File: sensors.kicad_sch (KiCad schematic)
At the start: 246 parts, among them K1 DRV5055A3xDBZxQ1, K10 DRV5055A3xDBZxQ1, K11 DRV5055A3xDBZxQ1, K12 DRV5055A3xDBZxQ1, K13 DRV5055A3xDBZxQ1, K14 DRV5055A3xDBZxQ1, K15 DRV5055A3xDBZxQ1, K16 DRV5055A3xDBZxQ1, K17 DRV5055A3xDBZxQ1, K18 DRV5055A3xDBZxQ1, K19 DRV5055A3xDBZxQ1, K2 DRV5055A3xDBZxQ1, K20 DRV5055A3xDBZxQ1, K21 DRV5055A3xDBZxQ1, K22 DRV5055A3xDBZxQ1, K23 DRV5055A3xDBZxQ1, K24 DRV5055A3xDBZxQ1, K25 DRV5055A3xDBZxQ1, K26 DRV5055A3xDBZxQ1, K27 DRV5055A3xDBZxQ1, K28 DRV5055A3xDBZxQ1, K29 DRV5055A3xDBZxQ1, K3 DRV5055A3xDBZxQ1, K30 DRV5055A3xDBZxQ1, K31 DRV5055A3xDBZxQ1, K32 DRV5055A3xDBZxQ1, K33 DRV5055A3xDBZxQ1, K34 DRV5055A3xDBZxQ1, K35 DRV5055A3xDBZxQ1, K36 DRV5055A3xDBZxQ1, K37 DRV5055A3xDBZxQ1, K38 DRV5055A3xDBZxQ1, K39 DRV5055A3xDBZxQ1, K4 DRV5055A3xDBZxQ1, K40 DRV5055A3xDBZxQ1, K41 DRV5055A3xDBZxQ1, K42 DRV5055A3xDBZxQ1, K43 DRV5055A3xDBZxQ1, K44 DRV5055A3xDBZxQ1, K45 DRV5055A3xDBZxQ1, K46 DRV5055A3xDBZxQ1, K47 DRV5055A3xDBZxQ1, K48 DRV5055A3xDBZxQ1, K49 DRV5055A3xDBZxQ1, K5 DRV5055A3xDBZxQ1, K50 DRV5055A3xDBZxQ1, K51 DRV5055A3xDBZxQ1, K52 DRV5055A3xDBZxQ1, K53 DRV5055A3xDBZxQ1, K54 DRV5055A3xDBZxQ1, K55 DRV5055A3xDBZxQ1, K56 DRV5055A3xDBZxQ1, K57 DRV5055A3xDBZxQ1, K58 DRV5055A3xDBZxQ1, K59 DRV5055A3xDBZxQ1, K6 DRV5055A3xDBZxQ1, K60 DRV5055A3xDBZxQ1, K61 DRV5055A3xDBZxQ1, K62 DRV5055A3xDBZxQ1, K63 DRV5055A3xDBZxQ1, K64 DRV5055A3xDBZxQ1, K65 DRV5055A3xDBZxQ1, K66 DRV5055A3xDBZxQ1, K67 DRV5055A3xDBZxQ1, K68 DRV5055A3xDBZxQ1, K69 DRV5055A3xDBZxQ1, K7 DRV5055A3xDBZxQ1, K70 DRV5055A3xDBZxQ1, K71 DRV5055A3xDBZxQ1, K72 DRV5055A3xDBZxQ1, K73 DRV5055A3xDBZxQ1, K74 DRV5055A3xDBZxQ1, K75 DRV5055A3xDBZxQ1, K76 DRV5055A3xDBZxQ1, K77 DRV5055A3xDBZxQ1, K78 DRV5055A3xDBZxQ1, K79 DRV5055A3xDBZxQ1, K8 DRV5055A3xDBZxQ1, K80 DRV5055A3xDBZxQ1, K81 DRV5055A3xDBZxQ1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

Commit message: add capacitor to mux vcc
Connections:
- net K1_OUT: no longer C10.2, C12.2, C14.2, C16.2, C18.2, C20.2, C22.2, C24.2, C26.2, C28.2, C30.2, C32.2, C4.2, C6.2, C8.2, K10.2 (OUT), K11.2 (OUT), K12.2 (OUT), K13.2 (OUT), K14.2 (OUT), K15.2 (OUT), K16.2 (OUT), K2.2 (OUT), K3.2 (OUT), K4.2 (OUT), K5.2 (OUT), K6.2 (OUT), K7.2 (OUT), K8.2 (OUT), K9.2 (OUT)
- new net K10_OUT: C20.2, K10.2 (OUT)
- new net K11_OUT: C22.2, K11.2 (OUT)
- new net K12_OUT: C24.2, K12.2 (OUT)
- new net K13_OUT: C26.2, K13.2 (OUT)
- new net K14_OUT: C28.2, K14.2 (OUT)
- new net K15_OUT: C30.2, K15.2 (OUT)
- new net K16_OUT: C32.2, K16.2 (OUT)
- new net K2_OUT: C4.2, K2.2 (OUT)
- new net K3_OUT: C6.2, K3.2 (OUT)
- new net K4_OUT: C8.2, K4.2 (OUT)
- new net K5_OUT: C10.2, K5.2 (OUT)
- new net K6_OUT: C12.2, K6.2 (OUT)
- new net K7_OUT: C14.2, K7.2 (OUT)
- new net K8_OUT: C16.2, K8.2 (OUT)
- new net K9_OUT: C18.2, K9.2 (OUT)
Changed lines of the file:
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@@
 		)
 	)
-	(global_label "K1_OUT"
+	(global_label "K16_OUT"
 		(shape input)
 		(at 417.83 68.58 90)
@@
 		)
 		(property "Intersheetrefs" "${INTERSHEET_REFS}"
-			(at 417.83 58.5191 90)
-			(effects
-				(font
-					(size 1.27 1.27)
-				)
-				(justify left)
-				(hide yes)
-			)
-		)
-	)
-	(global_label "K1_OUT"
+			(at 417.83 57.3096 90)
+			(effects
+				(font
+					(size 1.27 1.27)
+				)
+				(justify left)
+				(hide yes)
+			)
+		)
+	)
+	(global_label "K3_OUT"
 		(shape input)
 		(at 162.56 31.75 90)
@@
 		)
 	)
-	(global_label "K1_OUT"
+	(global_label "K15_OUT"
 		(shape input)
 		(at 367.03 68.58 90)
@@
 		)
 		(property "Intersheetrefs" "${INTERSHEET_REFS}"
-			(at 367.03 58.5191 90)
+			(at 367.03 57.3096 90)
 			(effects
 				(font
@@
 		)
 	)
-	(global_label "K1_OUT"
+	(global_label "K10_OUT"
 		(shape input)
 		(at 111.76 68.58 90)
@@
 		)
 		(property "Intersheetrefs" "${INTERSHEET_REFS}"
-			(at 111.76 58.5191 90)
+			(at 111.76 57.3096 90)
 			(effects
 				(font
@@
 		)
 	)
-	(global_label "K1_OUT"
+	(global_label "K7_OUT"
 		(shape input)
 		(at 367.03 31.75 90)
@@
 		)
 	)
-	(global_label "K1_OUT"
+	(global_label "K11_OUT"
 		(shape input)
 		(at 162.56 68.58 90)
@@
 		)
 		(property "Intersheetrefs" "${INTERSHEET_REFS}"
-			(at 162.56 58.5191 90)
+			(at 162.56 57.3096 90)
 			(effects
 				(font
@@
 		)
 	)
-	(global_label "K1_OUT"
+	(global_label "K14_OUT"
 		(shape input)
 		(at 316.23 68.58 90)
@@
 		)
 		(property "Intersheetrefs" "${INTERSHEET_REFS}"
-			(at 316.23 58.5191 90)
-			(effects
-				(font
-					(size 1.27 1.27)
-				)
-				(justify left)
-				(hide yes)
-			)
-		)
-	)
-	(global_label "K1_OUT"
+			(at 316.23 57.3096 90)
+			(effects
+				(font
+					(size 1.27 1.27)
+				)
+				(justify left)
+				(hide yes)
+			)
+		)
+	)
+	(global_label "K6_OUT"
 		(shape input)
 		(at 316.23 31.75 90)
@@
 		)
 	)
-	(global_label "K1_OUT"
+	(global_label "K2_OUT"
 		(shape input)
 		(at 111.76 31.75 90)
@@
 		)
 	)
-	(global_label "K1_OUT"
+	(global_label "K4_OUT"
 		(shape input)
 		(at 213.36 31.75 90)
@@
 		)
 	)
-	(global_label "K1_OUT"
+	(global_label "K9_OUT"
 		(shape input)
 		(at 60.96 68.58 90)
@@
 		)
 	)
-	(global_label "K1_OUT"
+	(global_label "K5_OUT"
 		(shape input)
 		(at 265.43 31.75 90)
@@
 		)
 	)
-	(global_label "K1_OUT"
+	(global_label "K13_OUT"
 		(shape input)
 		(at 265.43 68.58 90)
@@
 		)
 		(property "Intersheetrefs" "${INTERSHEET_REFS}"
-			(at 265.43 58.5191 90)
+			(at 265.43 57.3096 90)
 			(effects
 				(font
@@
 		)
 	)
-	(global_label "K1_OUT"
+	(global_label "K8_OUT"
 		(shape input)
 		(at 417.83 31.75 90)
@@
 		)
 	)
-	(global_label "K1_OUT"
+	(global_label "K12_OUT"
 		(shape input)
 		(at 213.36 68.58 90)
@@
 		)
 		(property "Intersheetrefs" "${INTERSHEET_REFS}"
-			(at 213.36 58.5191 90)
-			(effects
-				(font
+			(at 213.36 57.3096 90)
+			(effects
+				(font

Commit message: start placing mcu capacitor
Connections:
- net K1_OUT: no longer C106.2, C107.2, C108.2, C109.2, C116.2, C117.2, C118.2, C119.2, C126.2, C127.2, C128.2, C129.2, C136.2, C137.2, C138.2, C139.2, C146.2, C147.2, C148.2, C149.2, C156.2, C157.2, C158.2, C159.2, C34.2, C36.2, C38.2, C40.2, C42.2, C44.2, C46.2, C48.2, C50.2, C52.2, C54.2, C56.2, C58.2, C60.2, C62.2, C64.2, C66.2, C68.2, C70.2, C72.2, C74.2, C76.2, C78.2, C80.2, C86.2, C87.2, C88.2, C89.2, C90.2, C96.2, C97.2, C98.2, C99.2, K17.2 (OUT), K18.2 (OUT), K19.2 (OUT), K20.2 (OUT), K21.2 (OUT), K22.2 (OUT), K23.2 (OUT), K24.2 (OUT), K25.2 (OUT), K26.2 (OUT), K27.2 (OUT), K28.2 (OUT), K29.2 (OUT), K30.2 (OUT), K31.2 (OUT), K32.2 (OUT), K33.2 (OUT), K34.2 (OUT), K35.2 (OUT), K36.2 (OUT), K37.2 (OUT), K38.2 (OUT), K39.2 (OUT), K40.2 (OUT), K41.2 (OUT), K42.2 (OUT), K43.2 (OUT), K44.2 (OUT), K45.2 (OUT), K46.2 (OUT), K47.2 (OUT), K48.2 (OUT), K49.2 (OUT), K51.2 (OUT), K52.2 (OUT), K53.2 (OUT), K54.2 (OUT), K56.2 (OUT), K57.2 (OUT), K58.2 (OUT), K59.2 (OUT), K61.2 (OUT), K62.2 (OUT), K63.2 (OUT), K64.2 (OUT), K66.2 (OUT), K67.2 (OUT), K68.2 (OUT), K69.2 (OUT), K71.2 (OUT), K72.2 (OUT), K73.2 (OUT), K74.2 (OUT), K76.2 (OUT), K77.2 (OUT), K78.2 (OUT), K79.2 (OUT)
- new net K17_OUT: C34.2, K17.2 (OUT)
- new net K18_OUT: C36.2, K18.2 (OUT)
- new net K19_OUT: C38.2, K19.2 (OUT)
- new net K20_OUT: C40.2, K20.2 (OUT)
- new net K21_OUT: C42.2, K21.2 (OUT)
- new net K22_OUT: C44.2, K22.2 (OUT)
- new net K23_OUT: C46.2, K23.2 (OUT)
- new net K24_OUT: C48.2, K24.2 (OUT)
- new net K25_OUT: C50.2, K25.2 (OUT)
- new net K26_OUT: C52.2, K26.2 (OUT)
- new net K27_OUT: C54.2, K27.2 (OUT)
- new net K28_OUT: C56.2, K28.2 (OUT)
- new net K29_OUT: C58.2, K29.2 (OUT)
- new net K30_OUT: C60.2, K30.2 (OUT)
- new net K31_OUT: C62.2, K31.2 (OUT)
- new net K32_OUT: C64.2, K32.2 (OUT)
- new net K33_OUT: C66.2, K33.2 (OUT)
- new net K34_OUT: C68.2, K34.2 (OUT)
- new net K35_OUT: C70.2, K35.2 (OUT)
- new net K36_OUT: C72.2, K36.2 (OUT)
- new net K37_OUT: C74.2, K37.2 (OUT)
- new net K38_OUT: C76.2, K38.2 (OUT)
- new net K39_OUT: C78.2, K39.2 (OUT)
- new net K40_OUT: C80.2, K40.2 (OUT)
- new net K41_OUT: C86.2, K41.2 (OUT)
- new net K42_OUT: C87.2, K42.2 (OUT)
- new net K43_OUT: C88.2, K43.2 (OUT)
- new net K44_OUT: C89.2, K44.2 (OUT)
- new net K45_OUT: C90.2, K45.2 (OUT)
- new net K46_OUT: C96.2, K46.2 (OUT)
- new net K47_OUT: C97.2, K47.2 (OUT)
- new net K48_OUT: C98.2, K48.2 (OUT)
- new net K49_OUT: C99.2, K49.2 (OUT)
- new net K51_OUT: C106.2, K51.2 (OUT)
- new net K52_OUT: C107.2, K52.2 (OUT)
- new net K53_OUT: C108.2, K53.2 (OUT)
- new net K54_OUT: C109.2, K54.2 (OUT)
- new net K56_OUT: C116.2, K56.2 (OUT)
- new net K57_OUT: C117.2, K57.2 (OUT)
- new net K58_OUT: C118.2, K58.2 (OUT)
- new net K59_OUT: C119.2, K59.2 (OUT)
- new net K61_OUT: C126.2, K61.2 (OUT)
- new net K62_OUT: C127.2, K62.2 (OUT)
- new net K63_OUT: C128.2, K63.2 (OUT)
- new net K64_OUT: C129.2, K64.2 (OUT)
- new net K66_OUT: C136.2, K66.2 (OUT)
- new net K67_OUT: C137.2, K67.2 (OUT)
- new net K68_OUT: C138.2, K68.2 (OUT)
- new net K69_OUT: C139.2, K69.2 (OUT)
- new net K71_OUT: C146.2, K71.2 (OUT)
- new net K72_OUT: C147.2, K72.2 (OUT)
- new net K73_OUT: C148.2, K73.2 (OUT)
- new net K74_OUT: C149.2, K74.2 (OUT)
- new net K77_OUT: C157.2, K77.2 (OUT)
- new net K78_OUT: C156.2, C158.2, K76.2 (OUT), K78.2 (OUT)
- new net K79_OUT: C159.2, K79.2 (OUT)
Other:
- moved on the sheet: C163, C164, K82

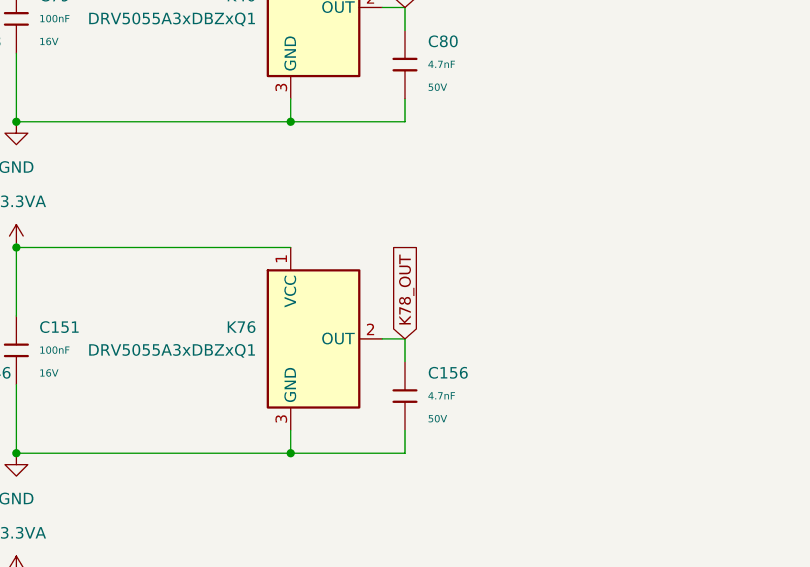
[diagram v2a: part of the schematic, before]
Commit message: finish sensor out capacitor
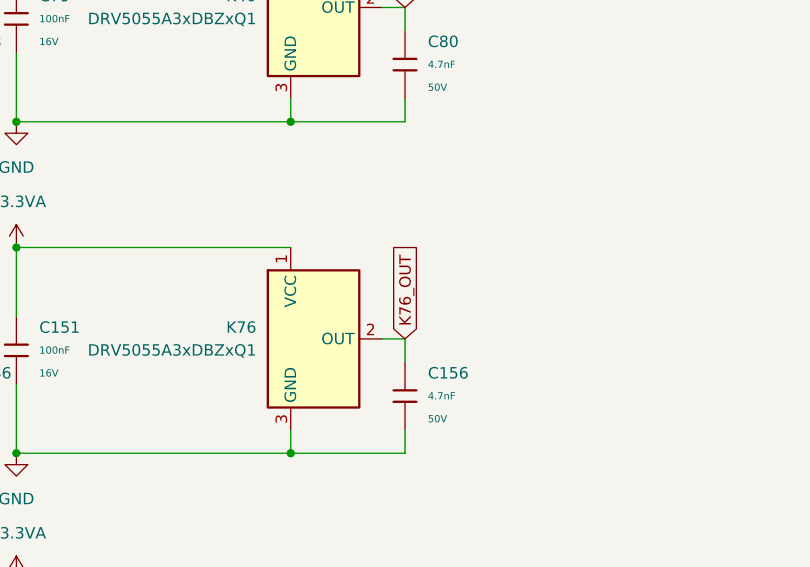
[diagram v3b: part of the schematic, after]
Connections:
- net K78_OUT: no longer C156.2, K76.2 (OUT)
- new net K76_OUT: C156.2, K76.2 (OUT)
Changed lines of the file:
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@@
 		)
 	)
-	(global_label "K78_OUT"
+	(global_label "K76_OUT"
 		(shape input)
 		(at 417.83 217.17 90)

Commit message: encodeur ajouté
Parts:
- added R204, R205, R206, R207, R208, R209, R210, R211, R212, R213, R214, R215, R216, R217, R218, R219, R220, R221, R222, R223, R224, R225, R226, R227, R228, R229, R230, R231, R232, R233, R234, R235, R236, R237, R238, R239, R240, R241, R242, R243, R244, R245, R246, R247, R248, R249, R250, R251, R252, R253, R254, R255, R256, R257, R258, R259, R260, R261, R262, R263, R264, R265, R266, R267, R268, R269, R270, R271, R272, R273, R274, R275, R276, R277, R278, R279, R280, R281, R282, R283, R284, R285: 470Ω, PCM_JLCPCB:R_0402, symbol PCM_JLCPCB-Resistors:0402,470Ω
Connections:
- net K10_OUT: now also R213.2; no longer K10.2 (OUT)
- net K11_OUT: now also R214.2; no longer K11.2 (OUT)
- net K12_OUT: now also R215.2; no longer K12.2 (OUT)
- net K13_OUT: now also R216.2; no longer K13.2 (OUT)
- net K14_OUT: now also R217.2; no longer K14.2 (OUT)
- net K15_OUT: now also R218.2; no longer K15.2 (OUT)
- net K16_OUT: now also R219.2; no longer K16.2 (OUT)
- net K17_OUT: now also R220.2; no longer K17.2 (OUT)
- net K18_OUT: now also R221.2; no longer K18.2 (OUT)
- net K19_OUT: now also R222.2; no longer K19.2 (OUT)
- net K1_OUT: now also R205.2; no longer K1.2 (OUT)
- net K20_OUT: now also R223.2; no longer K20.2 (OUT)
- net K21_OUT: now also R224.2; no longer K21.2 (OUT)
- net K22_OUT: now also R225.2; no longer K22.2 (OUT)
- net K23_OUT: now also R226.2; no longer K23.2 (OUT)
- net K24_OUT: now also R227.2; no longer K24.2 (OUT)
- net K25_OUT: now also R228.2; no longer K25.2 (OUT)
- net K26_OUT: now also R229.2; no longer K26.2 (OUT)
- net K27_OUT: now also R230.2; no longer K27.2 (OUT)
- net K28_OUT: now also R231.2; no longer K28.2 (OUT)
- net K29_OUT: now also R232.2; no longer K29.2 (OUT)
- net K2_OUT: now also R204.2; no longer K2.2 (OUT)
- net K30_OUT: now also R233.2; no longer K30.2 (OUT)
- net K31_OUT: now also R234.2; no longer K31.2 (OUT)
- net K32_OUT: now also R235.2; no longer K32.2 (OUT)
- net K33_OUT: now also R236.2; no longer K33.2 (OUT)
- net K34_OUT: now also R237.2; no longer K34.2 (OUT)
- net K35_OUT: now also R238.2; no longer K35.2 (OUT)
- net K36_OUT: now also R239.2; no longer K36.2 (OUT)
- net K37_OUT: now also R240.2; no longer K37.2 (OUT)
- net K38_OUT: now also R241.2; no longer K38.2 (OUT)
- net K39_OUT: now also R242.2; no longer K39.2 (OUT)
- net K3_OUT: now also R206.2; no longer K3.2 (OUT)
- net K40_OUT: now also R243.2; no longer K40.2 (OUT)
- net K41_OUT: now also R244.2; no longer K41.2 (OUT)
- net K42_OUT: now also R252.2; no longer K42.2 (OUT)
- net K43_OUT: now also R260.2; no longer K43.2 (OUT)
- net K44_OUT: now also R268.2; no longer K44.2 (OUT)
- net K45_OUT: now also R276.2; no longer K45.2 (OUT)
- net K46_OUT: now also R245.2; no longer K46.2 (OUT)
- net K47_OUT: now also R253.2; no longer K47.2 (OUT)
- net K48_OUT: now also R261.2; no longer K48.2 (OUT)
- net K49_OUT: now also R269.2; no longer K49.2 (OUT)
- net K4_OUT: now also R207.2; no longer K4.2 (OUT)
- net K50_OUT: now also R277.2; no longer K50.2 (OUT)
- net K51_OUT: now also R246.2; no longer K51.2 (OUT)
- net K52_OUT: now also R254.2; no longer K52.2 (OUT)
- net K53_OUT: now also R262.2; no longer K53.2 (OUT)
- net K54_OUT: now also R270.2; no longer K54.2 (OUT)
- net K55_OUT: now also R278.2; no longer K55.2 (OUT)
- net K56_OUT: now also R247.2; no longer K56.2 (OUT)
- net K57_OUT: now also R255.2; no longer K57.2 (OUT)
- net K58_OUT: now also R263.2; no longer K58.2 (OUT)
- net K59_OUT: now also R271.2; no longer K59.2 (OUT)
- net K5_OUT: now also R208.2; no longer K5.2 (OUT)
- net K60_OUT: now also R279.2; no longer K60.2 (OUT)
- net K61_OUT: now also R248.2; no longer K61.2 (OUT)
- net K62_OUT: now also R256.2; no longer K62.2 (OUT)
- net K63_OUT: now also R264.2; no longer K63.2 (OUT)
- net K64_OUT: now also R272.2; no longer K64.2 (OUT)
- net K65_OUT: now also R280.2; no longer K65.2 (OUT)
- net K66_OUT: now also R249.2; no longer K66.2 (OUT)
- net K67_OUT: now also R257.2; no longer K67.2 (OUT)
- net K68_OUT: now also R265.2; no longer K68.2 (OUT)
- net K69_OUT: now also R273.2; no longer K69.2 (OUT)
- net K6_OUT: now also R209.2; no longer K6.2 (OUT)
- net K70_OUT: now also R281.2; no longer K70.2 (OUT)
- net K71_OUT: now also R250.2; no longer K71.2 (OUT)
- net K72_OUT: now also R258.2; no longer K72.2 (OUT)
- net K73_OUT: now also R266.2; no longer K73.2 (OUT)
- net K74_OUT: now also R274.2; no longer K74.2 (OUT)
- net K75_OUT: now also R282.2; no longer K75.2 (OUT)
- net K76_OUT: now also R251.2; no longer K76.2 (OUT)
- net K77_OUT: now also R259.2; no longer K77.2 (OUT)
- net K78_OUT: now also R267.2; no longer K78.2 (OUT)
- net K79_OUT: now also R275.2; no longer K79.2 (OUT)
- net K7_OUT: now also R210.2; no longer K7.2 (OUT)
- net K80_OUT: now also R283.2; no longer K80.2 (OUT)
- net K81_OUT: now also R284.2; no longer K81.2 (OUT)
- net K82_OUT: now also R285.2; no longer K82.2 (OUT)
- net K8_OUT: now also R211.2; no longer K8.2 (OUT)
- net K9_OUT: now also R212.2; no longer K9.2 (OUT)
- new net: K12.2 (OUT), R215.1
- new net: K50.2 (OUT), R277.1
- new net: K37.2 (OUT), R240.1
- new net: K39.2 (OUT), R242.1
- new net: K64.2 (OUT), R272.1
- new net: K7.2 (OUT), R210.1
- new net: K24.2 (OUT), R227.1
- new net: K69.2 (OUT), R273.1
- new net: K3.2 (OUT), R206.1
- new net: K47.2 (OUT), R253.1
- new net: K55.2 (OUT), R278.1
- new net: K34.2 (OUT), R237.1
- new net: K23.2 (OUT), R226.1
- new net: K33.2 (OUT), R236.1
- new net: K14.2 (OUT), R217.1
- new net: K27.2 (OUT), R230.1
- new net: K35.2 (OUT), R238.1
- new net: K20.2 (OUT), R223.1
- new net: K77.2 (OUT), R259.1
- new net: K19.2 (OUT), R222.1
- new net: K26.2 (OUT), R229.1
- new net: K22.2 (OUT), R225.1
- new net: K56.2 (OUT), R247.1
- new net: K67.2 (OUT), R257.1
- new net: K1.2 (OUT), R205.1
- new net: K79.2 (OUT), R275.1
- new net: K16.2 (OUT), R219.1
- new net: K15.2 (OUT), R218.1
- new net: K4.2 (OUT), R207.1
- new net: K40.2 (OUT), R243.1
- new net: K59.2 (OUT), R271.1
- new net: K38.2 (OUT), R241.1
- new net: K70.2 (OUT), R281.1
- new net: K57.2 (OUT), R255.1
- new net: K49.2 (OUT), R269.1
- new net: K73.2 (OUT), R266.1
- new net: K25.2 (OUT), R228.1
- new net: K13.2 (OUT), R216.1
- new net: K36.2 (OUT), R239.1
- new net: K78.2 (OUT), R267.1
- new net: K54.2 (OUT), R270.1
- new net: K44.2 (OUT), R268.1
- new net: K62.2 (OUT), R256.1
- new net: K80.2 (OUT), R283.1
- new net: K43.2 (OUT), R260.1
- new net: K46.2 (OUT), R245.1
- new net: K5.2 (OUT), R208.1
- new net: K18.2 (OUT), R221.1
- new net: K82.2 (OUT), R285.1
- new net: K61.2 (OUT), R248.1
- new net: K66.2 (OUT), R249.1
- new net: K41.2 (OUT), R244.1
- new net: K75.2 (OUT), R282.1
- new net: K10.2 (OUT), R213.1
- new net: K11.2 (OUT), R214.1
- new net: K48.2 (OUT), R261.1
- new net: K76.2 (OUT), R251.1
- new net: K29.2 (OUT), R232.1
- new net: K45.2 (OUT), R276.1
- new net: K17.2 (OUT), R220.1
- new net: K42.2 (OUT), R252.1
- new net: K63.2 (OUT), R264.1
- new net: K32.2 (OUT), R235.1
- new net: K68.2 (OUT), R265.1
- new net: K9.2 (OUT), R212.1
- new net: K6.2 (OUT), R209.1
- new net: K28.2 (OUT), R231.1
- new net: K60.2 (OUT), R279.1
- new net: K52.2 (OUT), R254.1
- new net: K71.2 (OUT), R250.1
- new net: K72.2 (OUT), R258.1
- new net: K31.2 (OUT), R234.1
- new net: K65.2 (OUT), R280.1
- new net: K2.2 (OUT), R204.1
- new net: K58.2 (OUT), R263.1
- new net: K53.2 (OUT), R262.1
- new net: K74.2 (OUT), R274.1
- new net: K81.2 (OUT), R284.1
- new net: K21.2 (OUT), R224.1
- new net: K30.2 (OUT), R233.1
- new net: K8.2 (OUT), R211.1
- new net: K51.2 (OUT), R246.1
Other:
- moved on the sheet: K1, K10, K11, K12, K13, K14, K15, K16, K17, K18, K19, K2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

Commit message: Update 0402 resistors to 680Ω and add libs
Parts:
- C10, C100, C106, C107, C108, C109, C110, C116, C117, C118, C119, C12, C120, C126, C127, C128, C129, C130, C136, C137, C138, C139, C14, C140, C146, C147, C148, C149, C150, C156, C157, C158, C159, C16, C160, C162, C164, C18, C2, C20, C22, C24, C26, C28, C30, C32, C34, C36, C38, C4, C40, C42, C44, C46, C48, C50, C52, C54, C56, C58, C6, C60, C62, C64, C66, C68, C70, C72, C74, C76, C78, C8, C80, C86, C87, C88, C89, C90, C96, C97, C98, C99: value 4.7nF -> 22nF; symbol PCM_JLCPCB-Capacitors:0402,4.7nF -> PCM_JLCPCB-Capacitors:0402,22nF; Capacitance 4.7nF -> 22nF; LCSC C1538 -> C1532; Part 0402B472K500NT -> 0402B223K500NT; Stock 401641 -> 567776
- R204, R205, R206, R207, R208, R209, R210, R211, R212, R213, R214, R215, R216, R217, R218, R219, R220, R221, R222, R223, R224, R225, R226, R227, R228, R229, R230, R231, R232, R233, R234, R235, R236, R237, R238, R239, R240, R241, R242, R243, R244, R245, R246, R247, R248, R249, R250, R251, R252, R253, R254, R255, R256, R257, R258, R259, R260, R261, R262, R263, R264, R265, R266, R267, R268, R269, R270, R271, R272, R273, R274, R275, R276, R277, R278, R279, R280, R281, R282, R283, R284, R285: value 470Ω -> 680Ω; symbol PCM_JLCPCB-Resistors:0402,470Ω -> PCM_JLCPCB-Resistors:0402,680Ω; LCSC C25117 -> C25130; Part 0402WGF4700TCE -> 0402WGF6800TCE; Resistance 470Ω -> 680Ω; Stock 1007760 -> 315941

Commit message: Placed led
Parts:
- renumbered C78 to C100, C80 to C101, C81 to C102, C91 to C103, C101 to C104, C111 to C105, C121 to C106, C131 to C107, C141 to C108, C151 to C109, C86 to C110, C96 to C111, C106 to C112, C116 to C113, C126 to C114, C136 to C115, C146 to C116, C156 to C117, C82 to C118, C92 to C119, C102 to C120, C112 to C121, C132 to C123, C142 to C124, C152 to C125, C87 to C126, C97 to C127, C107 to C128, C117 to C129, C127 to C130, C137 to C131, C147 to C132, C157 to C133, C83 to C134, C93 to C135, C103 to C136, C113 to C137, C123 to C138, C133 to C139, C143 to C140, C153 to C141, C88 to C142, C98 to C143, C108 to C144, C118 to C145, C128 to C146, C138 to C147, C158 to C149, C84 to C150, C94 to C151, C104 to C152, C114 to C153, C124 to C154, C134 to C155, C144 to C156, C154 to C157, C89 to C158, C99 to C159, C109 to C160, C119 to C161, C129 to C162, C139 to C163, C149 to C164, C159 to C165, C161 to C166, C163 to C167, C162 to C168, C164 to C169, C85 to C170, C95 to C171, C105 to C172, C115 to C173, C125 to C174, C135 to C175, C145 to C176, C155 to C177, C90 to C178, C100 to C179, C110 to C180, C120 to C181, C130 to C182, C140 to C183, C150 to C184, C160 to C185, C1 to C22, C3 to C23, C5 to C24, C7 to C25, C9 to C26, C11 to C27, C13 to C28, C15 to C29, C2 to C30, C4 to C31, C6 to C32, C8 to C33, C10 to C34, C12 to C35, C14 to C36, C16 to C37, C17 to C38, C19 to C39, C21 to C40, C23 to C41, C25 to C42, C27 to C43, C29 to C44, C31 to C45, C18 to C46, C20 to C47, C22 to C48, C24 to C49, C26 to C50, C28 to C51, C30 to C52, C32 to C53, C33 to C54, C35 to C55, C37 to C56, C39 to C57, C41 to C58, C43 to C59, C45 to C60, C47 to C61, C34 to C62, C36 to C63, C38 to C64, C40 to C65, C42 to C66, C44 to C67, C46 to C68, C48 to C69, C49 to C70, C51 to C71, C53 to C72, C55 to C73, C57 to C74, C59 to C75, C61 to C76, C63 to C77, C50 to C78, C52 to C79, C54 to C80, C56 to C81, C58 to C82, C60 to C83, C62 to C84, C64 to C85, C65 to C86, C67 to C87, C69 to C88, C71 to C89, C73 to C90, C75 to C91, C77 to C92, C79 to C93, C66 to C94, C68 to C95, C70 to C96, C72 to C97, C74 to C98, C76 to C99, K46 to K42, K51 to K43, K56 to K44, K61 to K45, K66 to K46, K71 to K47, K76 to K48, K42 to K49, K47 to K50, K52 to K51, K57 to K52, K62 to K53, K67 to K54, K72 to K55, K77 to K56, K43 to K57, K48 to K58, K53 to K59, K58 to K60, K63 to K61, K68 to K62, K73 to K63, K78 to K64, K44 to K65, K49 to K66, K54 to K67, K59 to K68, K64 to K69, K69 to K70, K74 to K71, K79 to K72, K81 to K73, K82 to K74, K45 to K75, K50 to K76, K55 to K77, K60 to K78, K65 to K79, K70 to K80, K75 to K81, K80 to K82, R204 to R10, R206 to R11, R207 to R12, R208 to R13, R209 to R14, R210 to R15, R211 to R16, R212 to R17, R213 to R18, R214 to R19, R215 to R20, R216 to R21, R217 to R22, R218 to R23, R219 to R24, R220 to R25, R221 to R26, R222 to R27, R223 to R28, R224 to R29, R225 to R30, R226 to R31, R227 to R32, R228 to R33, R229 to R34, R230 to R35, R231 to R36, R232 to R37, R233 to R38, R234 to R39, R235 to R40, R236 to R41, R237 to R42, R238 to R43, R239 to R44, R240 to R45, R241 to R46, R242 to R47, R243 to R48, R244 to R49, R245 to R50, R246 to R51, R247 to R52, R248 to R53, R249 to R54, R250 to R55, R251 to R56, R252 to R57, R253 to R58, R254 to R59, R255 to R60, R256 to R61, R257 to R62, R258 to R63, R259 to R64, R260 to R65, R261 to R66, R262 to R67, R263 to R68, R264 to R69, R265 to R70, R266 to R71, R267 to R72, R268 to R73, R269 to R74, R270 to R75, R271 to R76, R272 to R77, R273 to R78, R274 to R79, R275 to R80, R284 to R81, R285 to R82, R276 to R83, R277 to R84, R278 to R85, R279 to R86, R280 to R87, R281 to R88, R282 to R89, R205 to R9, R283 to R90

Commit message: fix: sensors bad out label
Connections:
- net K46_OUT is gone; now on net K42_OUT: C111.2, R50.2
- net K42_OUT: no longer C126.2, R57.2
- net K43_OUT: now also C112.2, R51.2; no longer C142.2, R65.2
- net K44_OUT: now also C113.2, R52.2; no longer C158.2, R73.2
- net K45_OUT: now also C114.2, R53.2; no longer C178.2, R83.2
- net K47_OUT: now also C116.2, R55.2; no longer C127.2, R58.2
- net K48_OUT: now also C117.2, R56.2; no longer C143.2, R66.2
- net K49_OUT: now also C126.2, R57.2; no longer C159.2, R74.2
- net K50_OUT: now also C127.2, R58.2; no longer C179.2, R84.2
- net K51_OUT: now also C128.2, R59.2; no longer C112.2, R51.2
- net K52_OUT: now also C129.2, R60.2; no longer C128.2, R59.2
- net K53_OUT: now also C130.2, R61.2; no longer C144.2, R67.2
- net K54_OUT: now also C131.2, R62.2; no longer C160.2, R75.2
- net K55_OUT: now also C132.2, R63.2; no longer C180.2, R85.2
- net K56_OUT: now also C133.2, R64.2; no longer C113.2, R52.2
- net K57_OUT: now also C142.2, R65.2; no longer C129.2, R60.2
- net K58_OUT: now also C143.2, R66.2; no longer C145.2, R68.2
- net K59_OUT: now also C144.2, R67.2; no longer C161.2, R76.2
- net K60_OUT: now also C145.2, R68.2; no longer C181.2, R86.2
- net K61_OUT: now also C146.2, R69.2; no longer C114.2, R53.2
- net K62_OUT: now also C147.2, R70.2; no longer C130.2, R61.2
- net K63_OUT: now also C148.2, R71.2; no longer C146.2, R69.2
- net K64_OUT: now also C149.2, R72.2; no longer C162.2, R77.2
- net K65_OUT: now also C158.2, R73.2; no longer C182.2, R87.2
- net K66_OUT: now also C159.2, R74.2
- net K67_OUT: now also C160.2, R75.2; no longer C131.2, R62.2
- net K68_OUT: now also C161.2, R76.2; no longer C147.2, R70.2
- net K69_OUT: now also C162.2, R77.2; no longer C163.2, R78.2
- net K70_OUT: now also C163.2, R78.2; no longer C183.2, R88.2
- net K71_OUT: now also C164.2, R79.2; no longer C116.2, R55.2
- net K72_OUT: now also C165.2, R80.2; no longer C132.2, R63.2
- net K73_OUT: now also C168.2, R81.2; no longer C148.2, R71.2
- net K74_OUT: now also C169.2, R82.2; no longer C164.2, R79.2
- net K75_OUT: now also C178.2, R83.2; no longer C184.2, R89.2
- net K76_OUT: now also C179.2, R84.2; no longer C117.2, R56.2
- net K77_OUT: now also C180.2, R85.2; no longer C133.2, R64.2
- net K78_OUT: now also C181.2, R86.2; no longer C149.2, R72.2
- net K79_OUT: now also C182.2, R87.2; no longer C165.2, R80.2
- net K80_OUT: now also C183.2, R88.2; no longer C185.2, R90.2
- net K81_OUT: now also C184.2, R89.2; no longer C168.2, R81.2
- net K82_OUT: now also C185.2, R90.2; no longer C169.2, R82.2
